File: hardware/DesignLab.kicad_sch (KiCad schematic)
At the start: 87 parts

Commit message: Newly updated BOM
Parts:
- BT4: manf# 534-2477 -> 12BH343-GR
- SW13: manf# OS102011MA1QN1 -> TL3342F450QG
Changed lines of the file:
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@@
       (effects (font (size 1.27 1.27)) hide)
     )
-    (property "manf#" "534-2477" (id 5) (at 385.826 175.006 0)
+    (property "manf#" "12BH343-GR" (id 5) (at 385.826 175.006 0)
       (effects (font (size 1.27 1.27)) hide)
     )
@@
       (effects (font (size 1.27 1.27)) hide)
     )
-    (property "manf#" "OS102011MA1QN1" (id 5) (at 324.993 175.006 0)
+    (property "manf#" "TL3342F450QG" (id 5) (at 324.993 175.006 0)
       (effects (font (size 1.27 1.27)) hide)
     )
@@
     )
     (path "/b787c517-ecac-40e0-a211-870160b2f519"
-      (reference "BT4") (unit 1) (value "Battery_Cell") (footprint "Design:2477")
+      (reference "BT4") (unit 1) (value "Battery_Cell") (footprint "Connector_PinHeader_2.54mm:PinHeader_1x02_P2.54mm_Vertical")
     )
     (path "/902d9ee9-0c5c-4261-aa5f-66fe0365fde0"

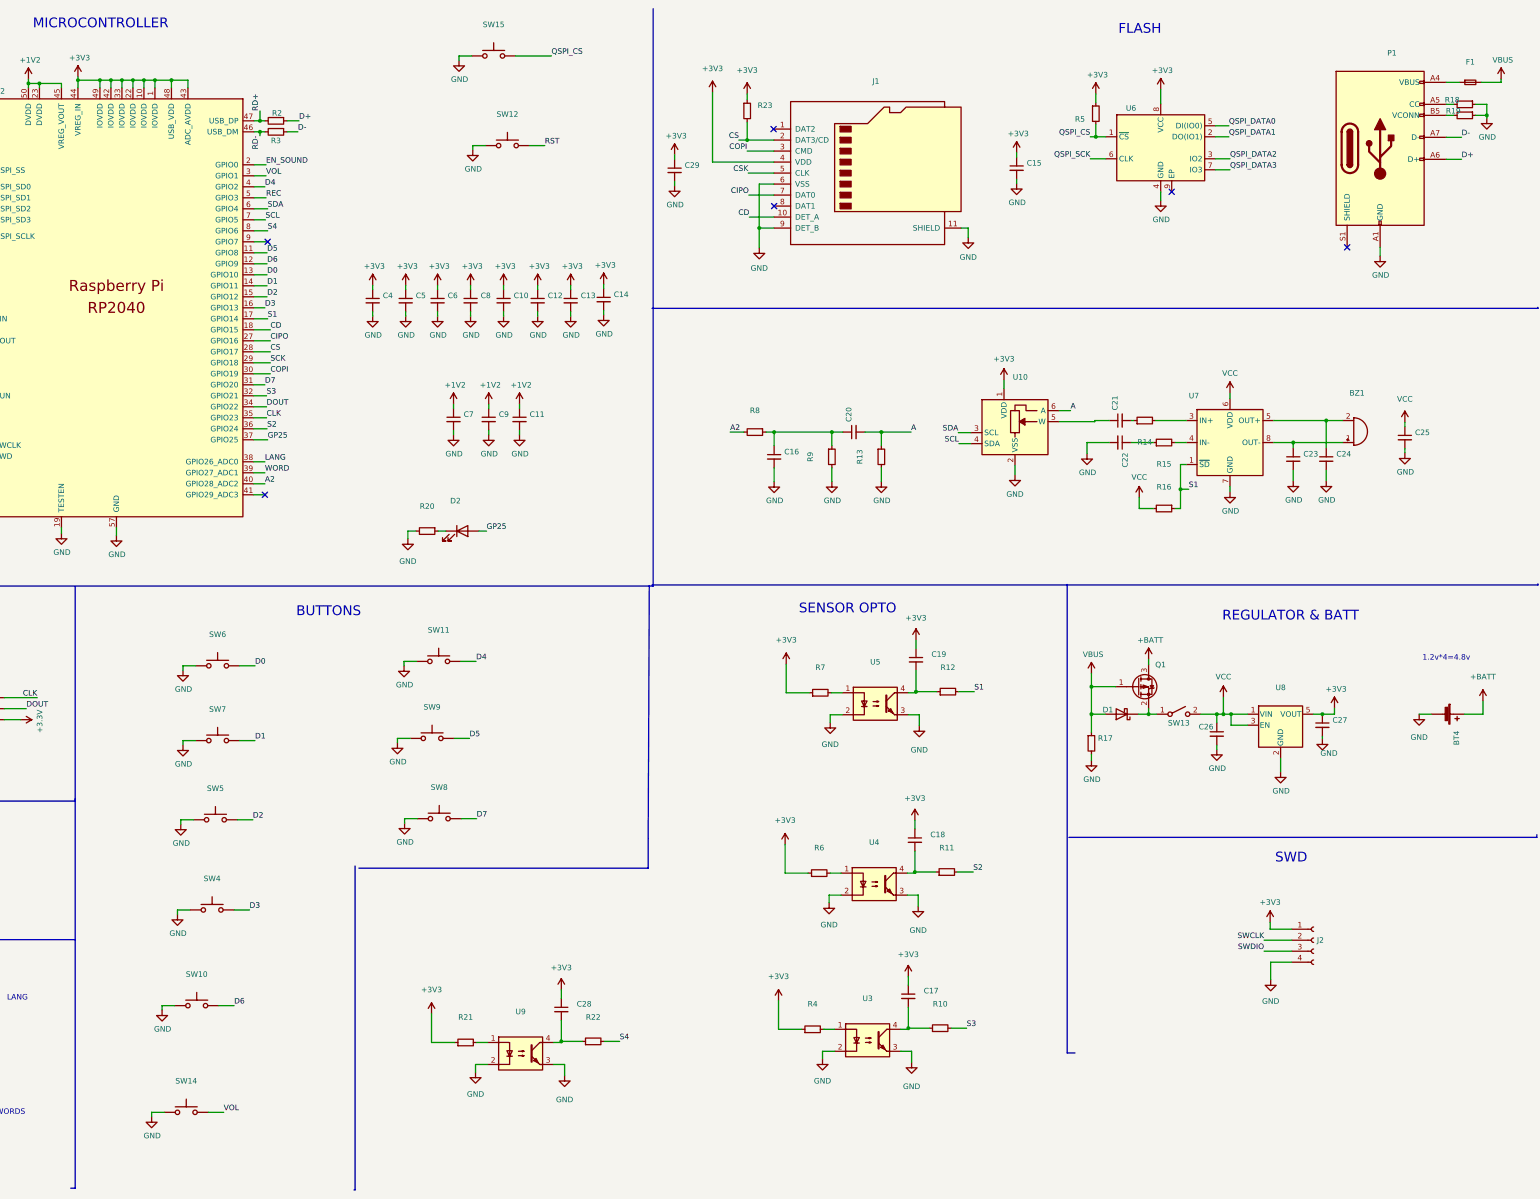
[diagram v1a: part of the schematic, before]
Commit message: Started routing and BOM corrected
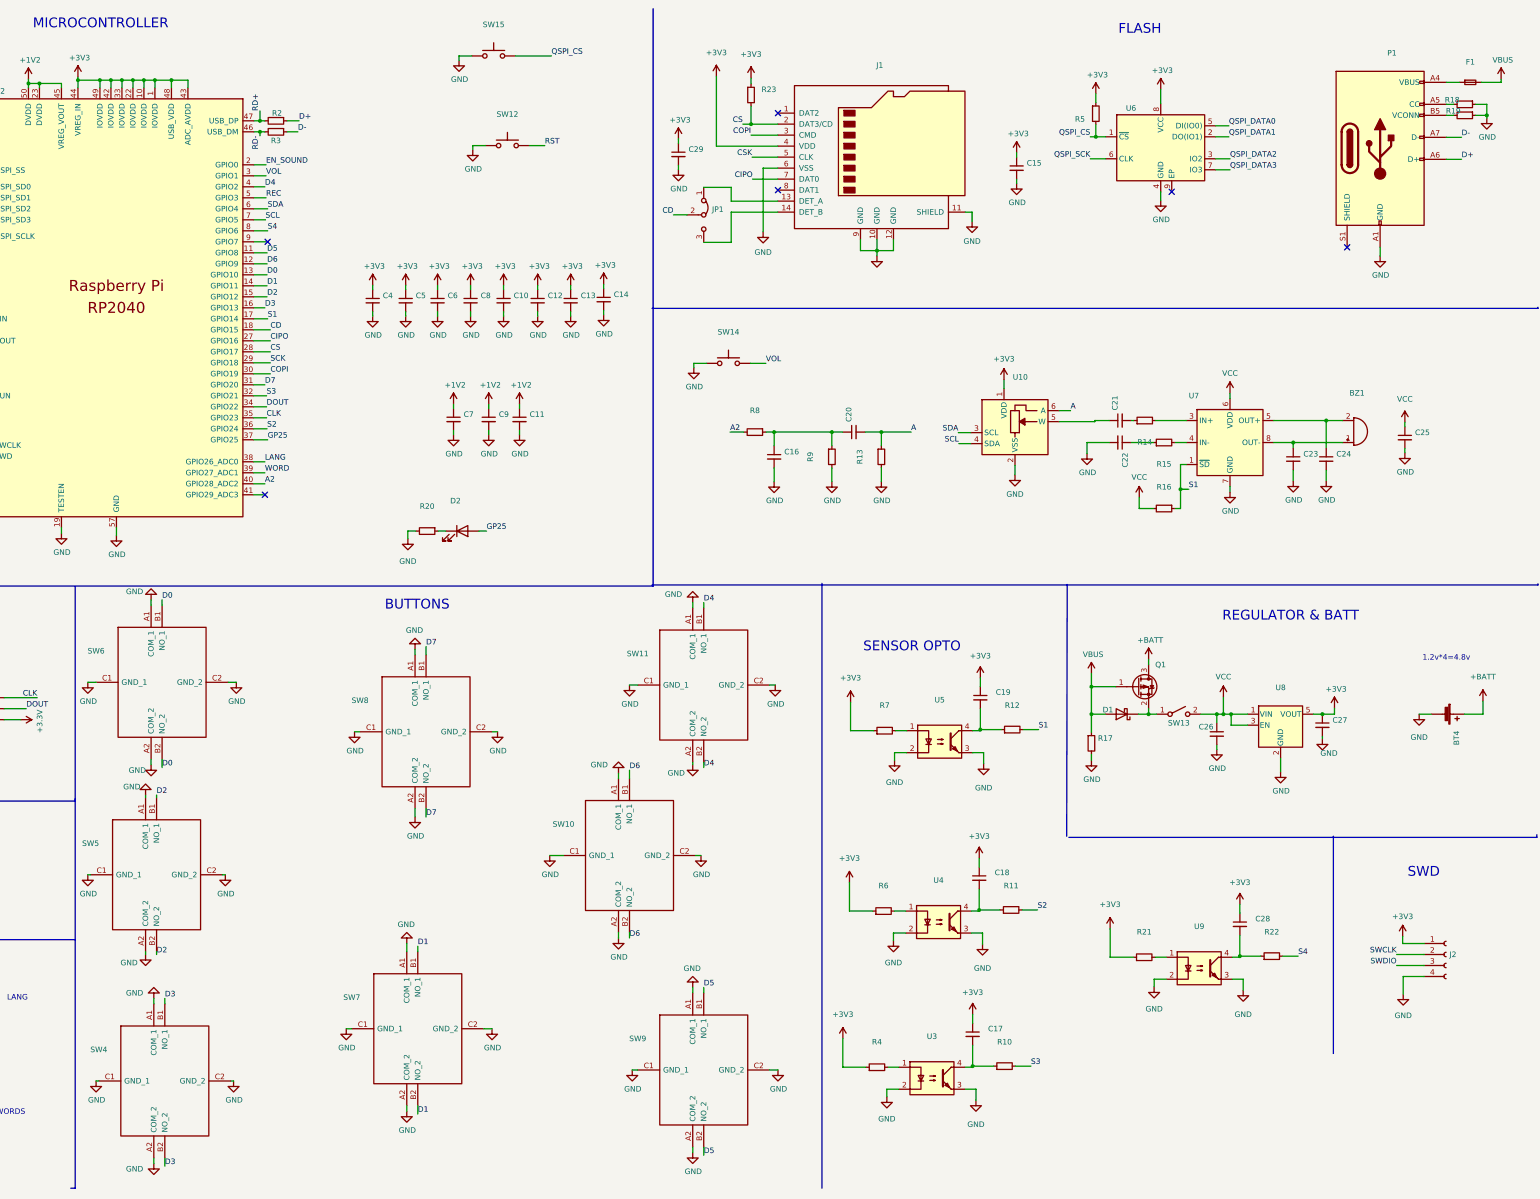
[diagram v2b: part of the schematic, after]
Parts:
- added JP1: (no value), symbol Jumper:Jumper_3_Bridged12
- J1: manf# OS102011MA1QN1 -> 1140084168
- SW10, SW11, SW4, SW5, SW6, SW7, SW8, SW9: symbol Switch:SW_Push -> EVQ-PLFA08:EVQ-PLFA08
- SW13: manf# TL3342F450QG -> OS102011MS2QN1
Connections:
- net CD: now also JP1.2 (C); no longer J1.10 (DET_A)
- net D0: now also SW6.B1 (NO_1), SW6.B2 (NO_2); no longer SW6.2
- net D1: now also SW7.B1 (NO_1), SW7.B2 (NO_2); no longer SW7.2
- net D2: now also SW5.B1 (NO_1), SW5.B2 (NO_2); no longer SW5.2
- net D3: now also SW4.B1 (NO_1), SW4.B2 (NO_2); no longer SW4.2
- net D4: now also SW11.B1 (NO_1), SW11.B2 (NO_2); no longer SW11.2
- net D5: now also SW9.B1 (NO_1), SW9.B2 (NO_2); no longer SW9.2
- net D6: now also SW10.B1 (NO_1), SW10.B2 (NO_2); no longer SW10.2
- net D7: now also SW8.B1 (NO_1), SW8.B2 (NO_2); no longer SW8.2
- net GND: now also J1.10 (GND), J1.12 (GND), SW10.A1 (COM_1), SW10.A2 (COM_2), SW10.C1 (GND_1), SW10.C2 (GND_2), SW11.A1 (COM_1), SW11.A2 (COM_2), SW11.C1 (GND_1), SW11.C2 (GND_2), SW4.A1 (COM_1), SW4.A2 (COM_2), SW4.C1 (GND_1), SW4.C2 (GND_2), SW5.A1 (COM_1), SW5.A2 (COM_2), SW5.C1 (GND_1), SW5.C2 (GND_2), SW6.A1 (COM_1), SW6.A2 (COM_2), SW6.C1 (GND_1), SW6.C2 (GND_2), SW7.A1 (COM_1), SW7.A2 (COM_2), SW7.C1 (GND_1), SW7.C2 (GND_2), SW8.A1 (COM_1), SW8.A2 (COM_2), SW8.C1 (GND_1), SW8.C2 (GND_2), SW9.A1 (COM_1), SW9.A2 (COM_2), SW9.C1 (GND_1), SW9.C2 (GND_2); no longer SW10.1, SW11.1, SW4.1, SW5.1, SW6.1, SW7.1, SW8.1, SW9.1
- new net: J1.13 (DET_A), JP1.1 (A)
- new net: J1.14 (DET_B), JP1.3 (B)
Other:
- moved on the sheet: C17, C18, C19, C28, C29, J2, R10, R11, R12, R21, R22, R23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

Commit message: Proposal PCB routing
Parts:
- BT4: value (none) -> Battery_Cell; footprint (none) -> Connector_PinHeader_2.54mm:PinHeader_1x02_P2.54mm_Vertical
- BZ1: value (none) -> Buzzer; footprint (none) -> Connector_PinHeader_2.54mm:PinHeader_1x02_P2.54mm_Vertical
- C1, C3: value (none) -> 27pF; footprint (none) -> Capacitor_SMD:C_0603_1608Metric
- C10, C11, C12, C13, C14, C15, C16, C5, C6, C8, C9: value (none) -> 100nF; footprint (none) -> Capacitor_SMD:C_0402_1005Metric_Pad0.74x0.62mm_HandSolder
- C17, C18, C19, C28: value (none) -> 10nF; footprint (none) -> Capacitor_SMD:C_0603_1608Metric
- C2: value (none) -> 0.1uF; footprint (none) -> Capacitor_SMD:C_0402_1005Metric_Pad0.74x0.62mm_HandSolder
- C20: value (none) -> 47uF; footprint (none) -> Capacitor_SMD:C_0603_1608Metric
- C21, C22, C4, C7: value (none) -> 1uF; footprint (none) -> Capacitor_SMD:C_0603_1608Metric
- C23, C24: value (none) -> 220pF; footprint (none) -> Capacitor_SMD:C_0603_1608Metric
- C25, C26, C27: value (none) -> 10uF; footprint (none) -> Capacitor_SMD:C_0402_1005Metric_Pad0.74x0.62mm_HandSolder
- C29: value (none) -> 100nF; footprint (none) -> Capacitor_SMD:C_0402_1005Metric
- D1: value (none) -> MBR120; footprint (none) -> Design:SODFL3616X98N
- D2: value (none) -> LED; footprint (none) -> Capacitor_SMD:C_0603_1608Metric
- F1: value (none) -> 0.5A; footprint (none) -> Fuse:Fuse_0805_2012Metric
- J1: value (none) -> Micro_SD_Card_Det; footprint (none) -> Design:1140084168
- J2: value (none) -> Conn_01x04_Female; footprint (none) -> Connector_PinHeader_2.54mm:PinHeader_1x04_P2.54mm_Vertical
- JP1: value (none) -> Jumper_3_Bridged12; footprint (none) -> Jumper:SolderJumper-3_P1.3mm_Bridged12_RoundedPad1.0x1.5mm
- P1: value (none) -> USB_C_Plug_USB2.0; footprint (none) -> Connectors:C393939
- Q1: value (none) -> DMG3415U-7; footprint (none) -> Package_TO_SOT_SMD:SOT-23
- R1: value (none) -> 1K; footprint (none) -> Resistor_SMD:R_0603_1608Metric
- R10, R11, R12, R22: value (none) -> 220; footprint (none) -> Capacitor_SMD:C_0603_1608Metric
- R13: value (none) -> 1.8K; footprint (none) -> Resistor_SMD:R_0603_1608Metric
- R14, R15, R9: value (none) -> 100; footprint (none) -> Resistor_SMD:R_0603_1608Metric
- R16: value (none) -> 10K; footprint (none) -> Resistor_SMD:R_0603_1608Metric
- R17, R23: value (none) -> 100K; footprint (none) -> Resistor_SMD:R_0603_1608Metric
- R18, R19: value (none) -> 5k1; footprint (none) -> Resistor_SMD:R_0603_1608Metric
- R2, R3: value (none) -> 27; footprint (none) -> Resistor_SMD:R_0603_1608Metric
- R20: value (none) -> 330; footprint (none) -> Resistor_SMD:R_0603_1608Metric
- R21, R4, R6, R7: value (none) -> 100; footprint (none) -> Capacitor_SMD:C_0603_1608Metric
- R5: value (none) -> 4K7; footprint (none) -> Resistor_SMD:R_0603_1608Metric
- R8: value (none) -> 220; footprint (none) -> Resistor_SMD:R_0603_1608Metric
- SW1, SW2: value (none) -> SW_DPDT_x2; footprint (none) -> Design:OS102011MA1QN1
- SW10, SW11, SW4, SW5, SW6, SW7, SW8, SW9: value (none) -> Button; footprint (none) -> Design:EVQPLFA08
- SW12: value (none) -> RESET; footprint (none) -> Button_Switch_SMD:SW_SPST_TL3342
- SW13: value (none) -> ON; footprint (none) -> Design:OS102011MA1QN1
- SW14: value (none) -> VOL; footprint (none) -> Button_Switch_SMD:SW_SPST_TL3342
- SW15: value (none) -> BOOT; footprint (none) -> Button_Switch_SMD:SW_SPST_TL3342
- SW3: value (none) -> REC; footprint (none) -> Button_Switch_SMD:SW_SPST_TL3342
- U1: value (none) -> SPH0641LM4H; footprint (none) -> Sensors:MIC_SPH0641LM4H-1
- U10: value (none) -> MCP4018-xxxxLT; footprint (none) -> Design:SOT65P210X110-6N
- U2: value (none) -> RP2040; footprint (none) -> badge_pwnCon:RP2040-QFN-56
- U3, U4, U5, U9: value (none) -> QRE1113; footprint (none) -> Design:QRE1113
- U6: value (none) -> AT25SF128A; footprint (none) -> Design:SOIC127P798X216-8N
- U7: value (none) -> PAM8302AAD; footprint (none) -> Package_SO:MSOP-8_3x3mm_P0.65mm
- U8: value (none) -> AP2112K-3.3; footprint (none) -> Package_TO_SOT_SMD:SOT-23-5
- Y1: value (none) -> 12Mhz; footprint (none) -> Crystal:Crystal_SMD_HC49-SD
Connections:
- net CSK is gone; now on net SCK: J1.5 (CLK)

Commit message: Routing corrected
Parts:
- BT4: value Battery_Cell -> (none); footprint Connector_PinHeader_2.54mm:PinHeader_1x02_P2.54mm_Vertical -> (none)
- BZ1: value Buzzer -> (none); footprint Connector_PinHeader_2.54mm:PinHeader_1x02_P2.54mm_Vertical -> (none)
- C1, C3: value 27pF -> (none); footprint Capacitor_SMD:C_0603_1608Metric -> (none)
- C10, C11, C12, C13, C14, C15, C16, C5, C6, C8, C9: value 100nF -> (none); footprint Capacitor_SMD:C_0402_1005Metric_Pad0.74x0.62mm_HandSolder -> (none)
- C17, C18, C19, C28: value 10nF -> (none); footprint Capacitor_SMD:C_0603_1608Metric -> (none)
- C2: value 0.1uF -> (none); footprint Capacitor_SMD:C_0402_1005Metric_Pad0.74x0.62mm_HandSolder -> (none)
- C20: value 47uF -> (none); footprint Capacitor_SMD:C_0603_1608Metric -> (none)
- C21, C22, C4, C7: value 1uF -> (none); footprint Capacitor_SMD:C_0603_1608Metric -> (none)
- C23, C24: value 220pF -> (none); footprint Capacitor_SMD:C_0603_1608Metric -> (none)
- C25, C26, C27: value 10uF -> (none); footprint Capacitor_SMD:C_0402_1005Metric_Pad0.74x0.62mm_HandSolder -> (none)
- C29: value 100nF -> (none); footprint Capacitor_SMD:C_0402_1005Metric -> (none)
- D1: value MBR120 -> (none); footprint Design:SODFL3616X98N -> (none)
- D2: value LED -> (none); footprint Capacitor_SMD:C_0603_1608Metric -> (none)
- F1: value 0.5A -> (none); footprint Fuse:Fuse_0805_2012Metric -> (none)
- J1: value Micro_SD_Card_Det -> (none); footprint Design:1140084168 -> (none)
- J2: value Conn_01x04_Female -> (none); footprint Connector_PinHeader_2.54mm:PinHeader_1x04_P2.54mm_Vertical -> (none)
- JP1: value Jumper_3_Bridged12 -> (none); footprint Jumper:SolderJumper-3_P1.3mm_Bridged12_RoundedPad1.0x1.5mm -> (none)
- P1: value USB_C_Plug_USB2.0 -> (none); footprint Connectors:C393939 -> (none)
- Q1: value DMG3415U-7 -> (none); footprint Package_TO_SOT_SMD:SOT-23 -> (none)
- R1: value 1K -> (none); footprint Resistor_SMD:R_0603_1608Metric -> (none)
- R10, R11, R12, R22: value 220 -> (none); footprint Capacitor_SMD:C_0603_1608Metric -> (none)
- R13: value 1.8K -> (none); footprint Resistor_SMD:R_0603_1608Metric -> (none)
- R14, R15, R9: value 100 -> (none); footprint Resistor_SMD:R_0603_1608Metric -> (none)
- R16: value 10K -> (none); footprint Resistor_SMD:R_0603_1608Metric -> (none)
- R17, R23: value 100K -> (none); footprint Resistor_SMD:R_0603_1608Metric -> (none)
- R18, R19: value 5k1 -> (none); footprint Resistor_SMD:R_0603_1608Metric -> (none)
- R2, R3: value 27 -> (none); footprint Resistor_SMD:R_0603_1608Metric -> (none)
- R20: value 330 -> (none); footprint Resistor_SMD:R_0603_1608Metric -> (none)
- R21, R4, R6, R7: value 100 -> (none); footprint Capacitor_SMD:C_0603_1608Metric -> (none)
- R5: value 4K7 -> (none); footprint Resistor_SMD:R_0603_1608Metric -> (none)
- R8: value 220 -> (none); footprint Resistor_SMD:R_0603_1608Metric -> (none)
- SW1, SW2: value SW_DPDT_x2 -> (none); footprint Design:OS102011MA1QN1 -> (none)
- SW10, SW11, SW4, SW5, SW6, SW7, SW8, SW9: value Button -> (none); footprint Design:EVQPLFA08 -> (none)
- SW12: value RESET -> (none); footprint Button_Switch_SMD:SW_SPST_TL3342 -> (none)
- SW13: value ON -> (none); footprint Design:OS102011MA1QN1 -> (none)
- SW14: value VOL -> (none); footprint Button_Switch_SMD:SW_SPST_TL3342 -> (none)
- SW15: value BOOT -> (none); footprint Button_Switch_SMD:SW_SPST_TL3342 -> (none)
- SW3: value REC -> (none); footprint Button_Switch_SMD:SW_SPST_TL3342 -> (none)
- U1: value SPH0641LM4H -> (none); footprint Sensors:MIC_SPH0641LM4H-1 -> (none)
- U10: value MCP4018-xxxxLT -> (none); footprint Design:SOT65P210X110-6N -> (none)
- U2: value RP2040 -> (none); footprint badge_pwnCon:RP2040-QFN-56 -> (none)
- U3, U4, U5, U9: value QRE1113 -> (none); footprint Design:QRE1113 -> (none)
- U6: value AT25SF128A -> (none); footprint Design:SOIC127P798X216-8N -> (none)
- U7: value PAM8302AAD -> (none); footprint Package_SO:MSOP-8_3x3mm_P0.65mm -> (none)
- U8: value AP2112K-3.3 -> (none); footprint Package_TO_SOT_SMD:SOT-23-5 -> (none)
- Y1: value 12Mhz -> (none); footprint Crystal:Crystal_SMD_HC49-SD -> (none)

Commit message: Button flipped
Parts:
- BT4: value (none) -> Battery_Cell; footprint (none) -> Connector_PinHeader_2.54mm:PinHeader_1x02_P2.54mm_Vertical
- BZ1: value (none) -> Buzzer; footprint (none) -> Connector_PinHeader_2.54mm:PinHeader_1x02_P2.54mm_Vertical
- C1, C3: value (none) -> 27pF; footprint (none) -> Capacitor_SMD:C_0603_1608Metric
- C10, C11, C12, C13, C14, C15, C16, C5, C6, C8, C9: value (none) -> 100nF; footprint (none) -> Capacitor_SMD:C_0402_1005Metric_Pad0.74x0.62mm_HandSolder
- C17, C18, C19, C28: value (none) -> 10nF; footprint (none) -> Capacitor_SMD:C_0603_1608Metric
- C2: value (none) -> 0.1uF; footprint (none) -> Capacitor_SMD:C_0402_1005Metric_Pad0.74x0.62mm_HandSolder
- C20: value (none) -> 47uF; footprint (none) -> Capacitor_SMD:C_0603_1608Metric
- C21, C22, C4, C7: value (none) -> 1uF; footprint (none) -> Capacitor_SMD:C_0603_1608Metric
- C23, C24: value (none) -> 220pF; footprint (none) -> Capacitor_SMD:C_0603_1608Metric
- C25, C26, C27: value (none) -> 10uF; footprint (none) -> Capacitor_SMD:C_0402_1005Metric_Pad0.74x0.62mm_HandSolder
- C29: value (none) -> 100nF; footprint (none) -> Capacitor_SMD:C_0402_1005Metric
- D1: value (none) -> MBR120; footprint (none) -> Design:SODFL3616X98N
- D2: value (none) -> LED; footprint (none) -> Capacitor_SMD:C_0603_1608Metric
- F1: value (none) -> 0.5A; footprint (none) -> Fuse:Fuse_0805_2012Metric
- J1: value (none) -> Micro_SD_Card_Det; footprint (none) -> Design:1140084168
- J2: value (none) -> Conn_01x04_Female; footprint (none) -> Connector_PinHeader_2.54mm:PinHeader_1x04_P2.54mm_Vertical
- JP1: value (none) -> Jumper_3_Bridged12; footprint (none) -> Jumper:SolderJumper-3_P1.3mm_Bridged12_RoundedPad1.0x1.5mm
- P1: value (none) -> USB_C_Plug_USB2.0; footprint (none) -> Connectors:C393939
- Q1: value (none) -> DMG3415U-7; footprint (none) -> Package_TO_SOT_SMD:SOT-23
- R1: value (none) -> 1K; footprint (none) -> Resistor_SMD:R_0603_1608Metric
- R10, R11, R12, R22: value (none) -> 220; footprint (none) -> Capacitor_SMD:C_0603_1608Metric
- R13: value (none) -> 1.8K; footprint (none) -> Resistor_SMD:R_0603_1608Metric
- R14, R15, R9: value (none) -> 100; footprint (none) -> Resistor_SMD:R_0603_1608Metric
- R16: value (none) -> 10K; footprint (none) -> Resistor_SMD:R_0603_1608Metric
- R17, R23: value (none) -> 100K; footprint (none) -> Resistor_SMD:R_0603_1608Metric
- R18, R19: value (none) -> 5k1; footprint (none) -> Resistor_SMD:R_0603_1608Metric
- R2, R3: value (none) -> 27; footprint (none) -> Resistor_SMD:R_0603_1608Metric
- R20: value (none) -> 330; footprint (none) -> Resistor_SMD:R_0603_1608Metric
- R21, R4, R6, R7: value (none) -> 100; footprint (none) -> Capacitor_SMD:C_0603_1608Metric
- R5: value (none) -> 4K7; footprint (none) -> Resistor_SMD:R_0603_1608Metric
- R8: value (none) -> 220; footprint (none) -> Resistor_SMD:R_0603_1608Metric
- SW1, SW2: value (none) -> SW_DPDT_x2; footprint (none) -> Design:OS102011MA1QN1
- SW10, SW11, SW4, SW5, SW6, SW7, SW8, SW9: value (none) -> Button; footprint (none) -> Design:EVQPLFA08
- SW12: value (none) -> RESET; footprint (none) -> Button_Switch_SMD:SW_SPST_TL3342
- SW13: value (none) -> ON; footprint (none) -> Design:OS102011MA1QN1
- SW14: value (none) -> VOL; footprint (none) -> Button_Switch_SMD:SW_SPST_TL3342
- SW15: value (none) -> BOOT; footprint (none) -> Button_Switch_SMD:SW_SPST_TL3342
- SW3: value (none) -> REC; footprint (none) -> Button_Switch_SMD:SW_SPST_TL3342
- U1: value (none) -> SPH0641LM4H; footprint (none) -> Sensors:MIC_SPH0641LM4H-1
- U10: value (none) -> MCP4018-xxxxLT; footprint (none) -> Design:SOT65P210X110-6N
- U2: value (none) -> RP2040; footprint (none) -> badge_pwnCon:RP2040-QFN-56
- U3, U4, U5, U9: value (none) -> QRE1113; footprint (none) -> Design:QRE1113
- U6: value (none) -> AT25SF128A; footprint (none) -> Design:SOIC127P798X216-8N
- U7: value (none) -> PAM8302AAD; footprint (none) -> Package_SO:MSOP-8_3x3mm_P0.65mm
- U8: value (none) -> AP2112K-3.3; footprint (none) -> Package_TO_SOT_SMD:SOT-23-5
- Y1: value (none) -> 12Mhz; footprint (none) -> Crystal:Crystal_SMD_HC49-SD
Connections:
- net GND: now also P1.S1 (SHIELD)
- no-connect marks 6 -> 5
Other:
- moved on the sheet: F1, P1, R18, R19
